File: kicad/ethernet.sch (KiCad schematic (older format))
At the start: 48 parts, among them U2 NUP4114UPXV6T1G, U3 NUP4114UPXV6T1G, X1 L829-1J1T-43

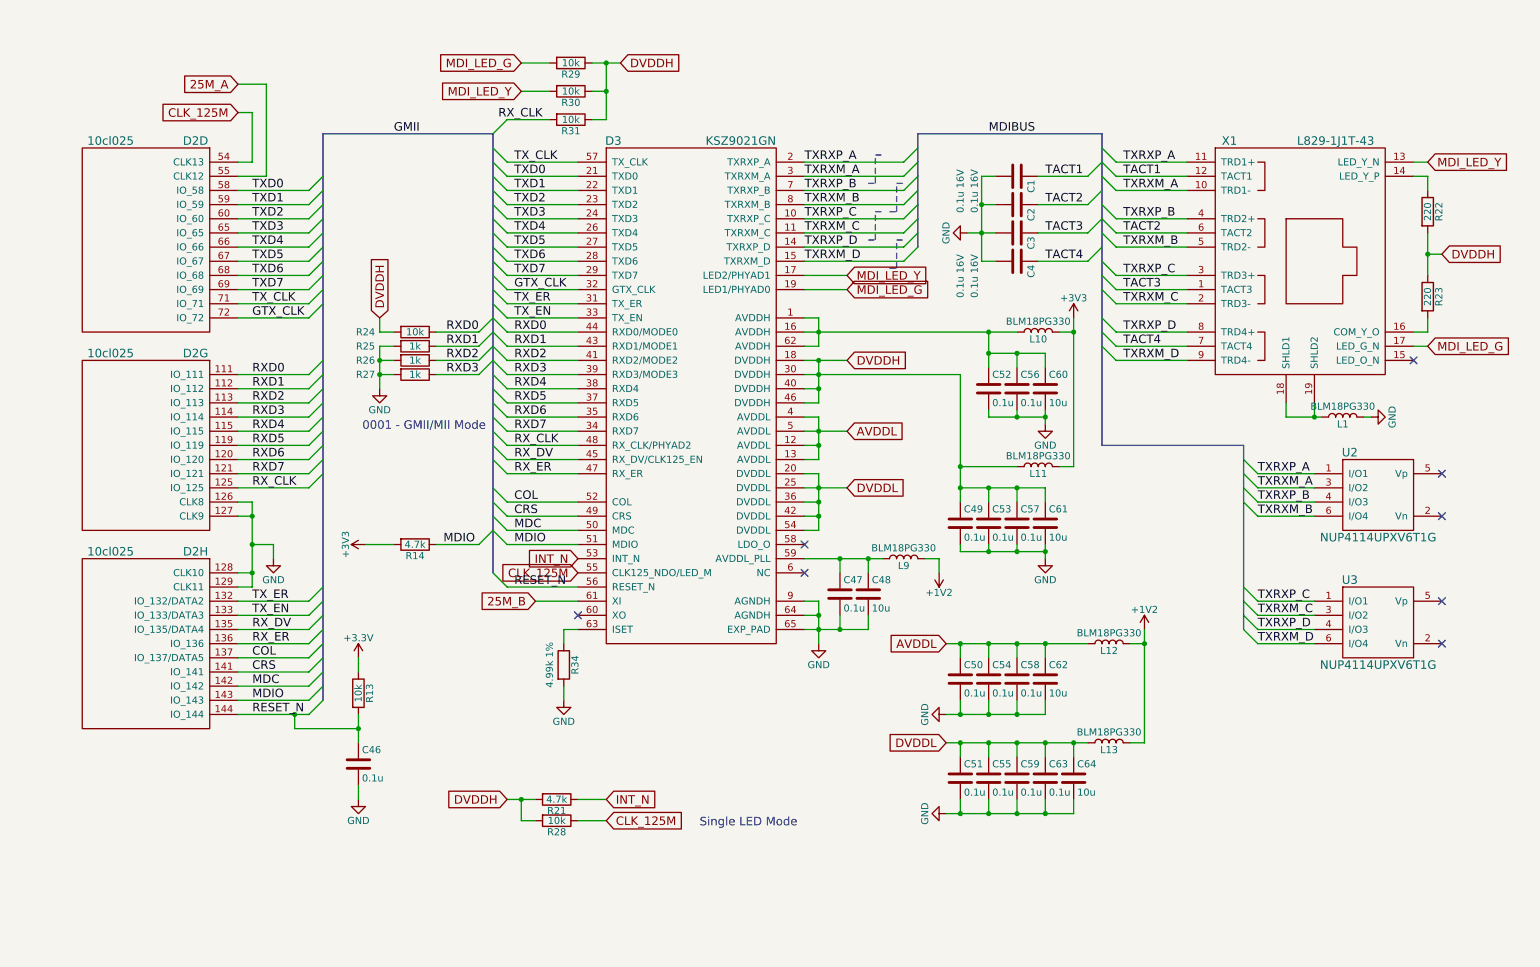
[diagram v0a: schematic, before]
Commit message: Project translated to template "Raspberry Pi HAT" Added library files from template. Renamed refdes. Changed placement for all components
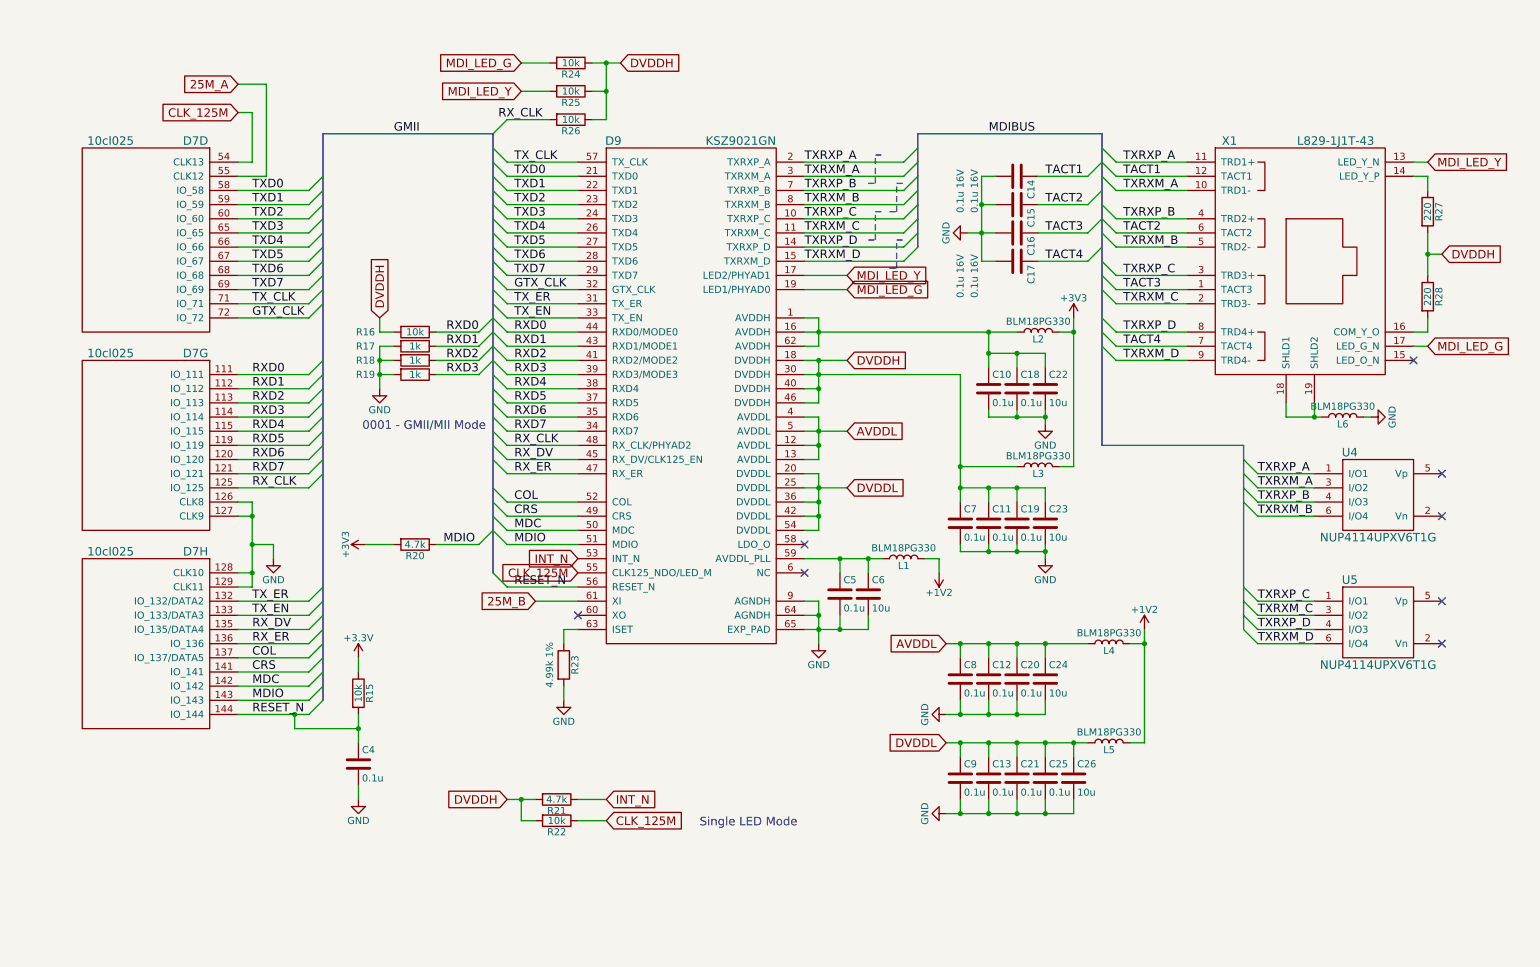
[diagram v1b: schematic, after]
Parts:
- renumbered C52 to C10, C53 to C11, C54 to C12, C55 to C13, C1 to C14, C2 to C15, C3 to C16, C4 to C17, C56 to C18, C57 to C19, C58 to C20, C59 to C21, C60 to C22, C61 to C23, C62 to C24, C63 to C25, C64 to C26, C46 to C4, C47 to C5, C48 to C6, C49 to C7, C50 to C8, C51 to C9, D2 to D7, D3 to D9, L9 to L1, L10 to L2, L11 to L3, L12 to L4, L13 to L5, L1 to L6, R13 to R15, R24 to R16, R25 to R17, R26 to R18, R27 to R19, R14 to R20, R28 to R22, R34 to R23, R29 to R24, R30 to R25, R31 to R26, R22 to R27, R23 to R28, U2 to U4, U3 to U5

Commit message: Schematics updated for correct BOM generation Corrected RefDes (not renumbered yet) PCB updated (not routed) Added 3d models for new components Added folder assy (empty) Added folder bom Added BOM file (bom/BOM_fpgagigepi.xls) Added datasheet for ocscillator 25MHz (datasheets/ASEMB.pdf)
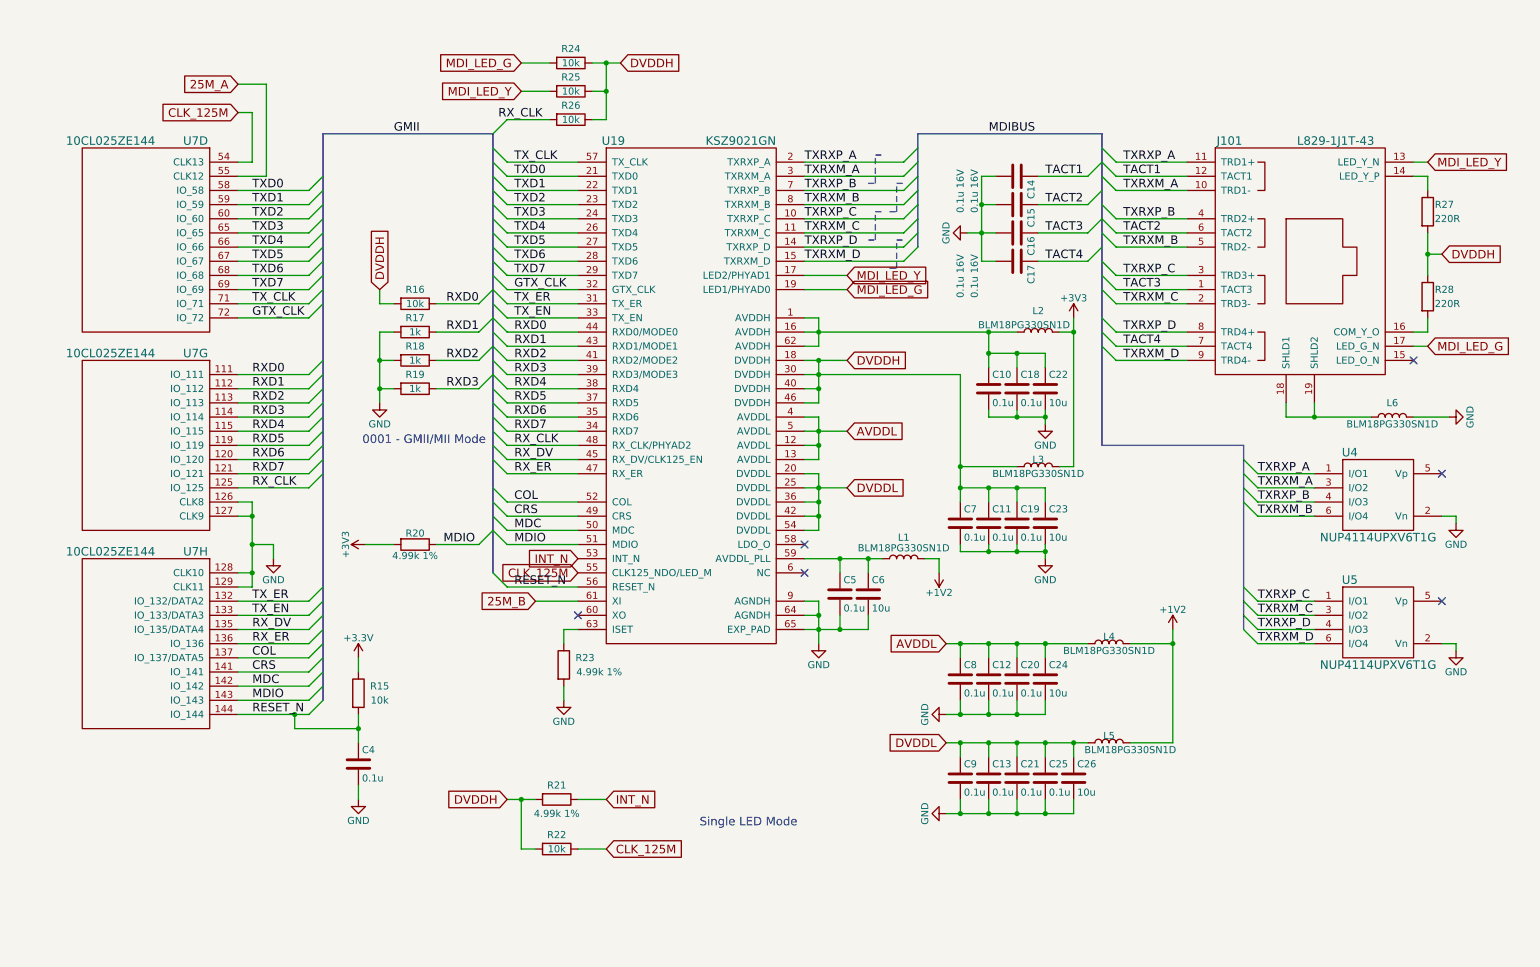
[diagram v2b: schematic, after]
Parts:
- C10, C11, C12, C13, C14, C15, C16, C17, C18, C19, C20, C21, C22, C23, C24, C25, C26, C4, C5, C6, C7, C8, C9: footprint Capacitors_SMD:C_0603_HandSoldering -> Capacitors_SMD:C_0603
- L1, L2, L3, L4, L5, L6: value BLM18PG330 -> BLM18PG330SN1D; footprint Inductors_SMD:L_0603_HandSoldering -> Inductors_SMD:L_0603
- R15, R16, R17, R18, R19, R22, R23, R24, R25, R26: footprint Resistors_SMD:R_0603_HandSoldering -> Resistors_SMD:R_0603
- R20, R21: value 4.7k -> 4.99k 1%; footprint Resistors_SMD:R_0603_HandSoldering -> Resistors_SMD:R_0603
- R27, R28: value 220 -> 220R; footprint Resistors_SMD:R_0603_HandSoldering -> Resistors_SMD:R_0603
- U7: renamed from D7; value 10cl025 -> 10CL025ZE144
- renumbered X1 to J101, D9 to U19
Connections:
- net GND: now also U4.2 (Vn), U5.2 (Vn)
- no-connect marks 8 -> 6
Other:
- moved on the sheet: L6, R16, R17, R19, R22

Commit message: Corrected path for schematics Renumbered components Remaped GMII connections to other banks PCB updated - final placement for major components and some conn routed Corrected 3d models Add text Cyclone 10LP Added 3d models for new components Added folder assy (empty) Added folder bom Added BOM file (bom/BOM_fpgagigepi.xls)
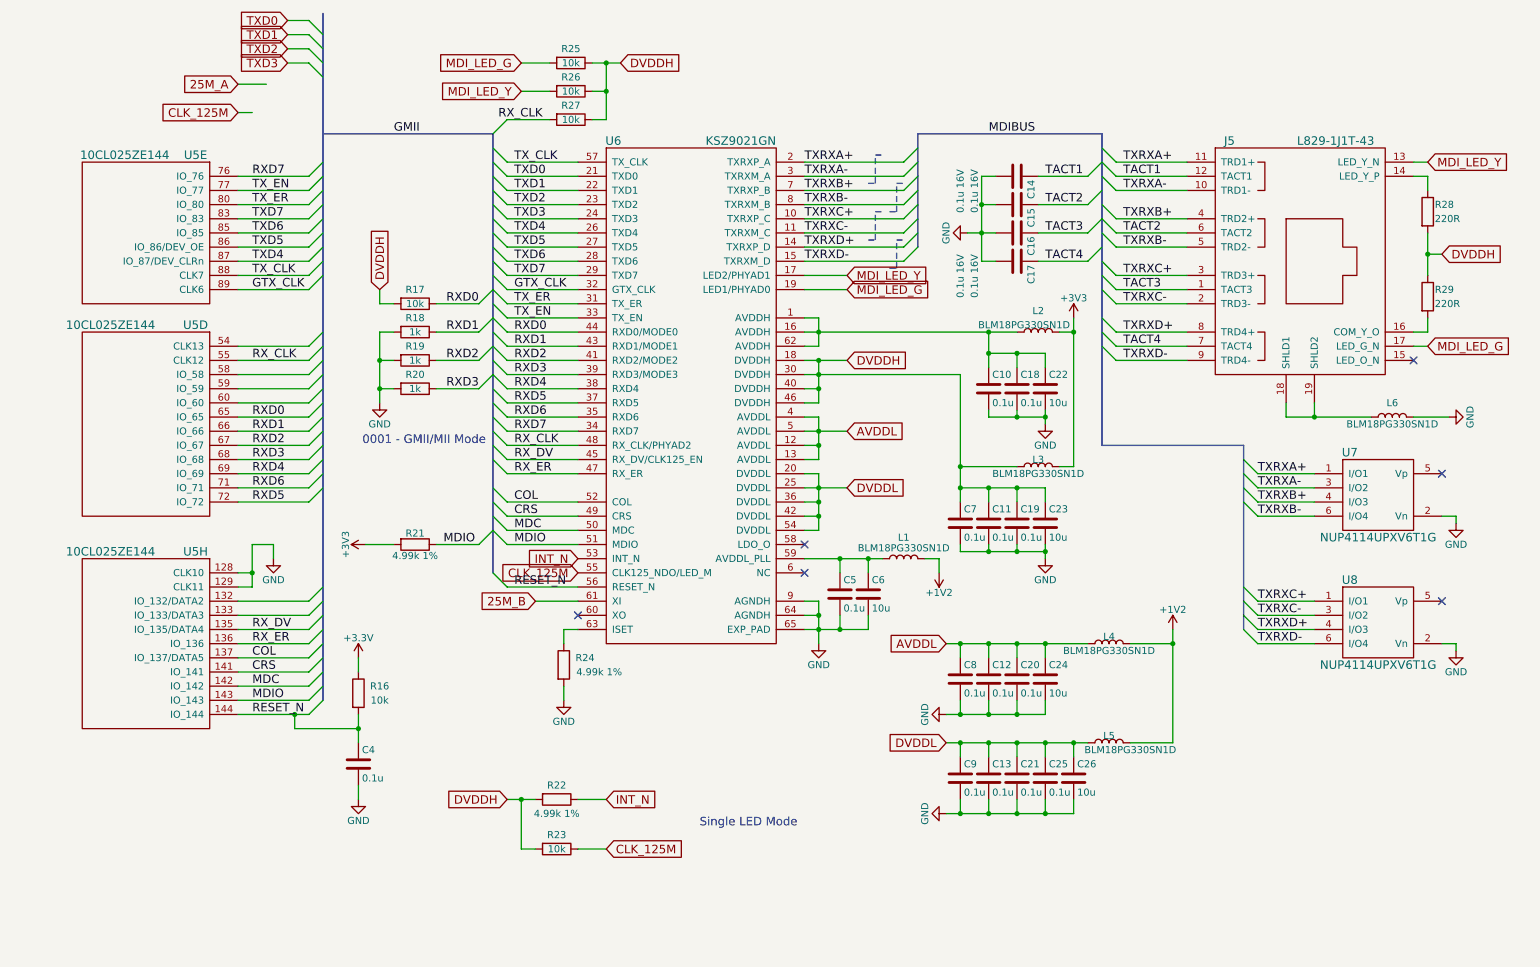
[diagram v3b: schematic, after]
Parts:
- renumbered J101 to J5, R15 to R16, R16 to R17, R17 to R18, R18 to R19, R19 to R20, R20 to R21, R21 to R22, R22 to R23, R23 to R24, R24 to R25, R25 to R26, R26 to R27, R27 to R28, R28 to R29, U7 to U5, U19 to U6, U4 to U7, U5 to U8
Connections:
- net 25M_A: no longer U5.55 (CLK12)
- net CLK_125M: no longer U5.54 (CLK13)
- net GND: no longer U5.126 (CLK8), U5.127 (CLK9)
- net GTX_CLK: now also U5.89 (CLK6); no longer U5.72 (IO_72)
- net RXD0: now also U5.65 (IO_65); no longer U5.111 (IO_111)
- net RXD1: now also U5.66 (IO_66); no longer U5.112 (IO_112)
- net RXD2: now also U5.67 (IO_67); no longer U5.113 (IO_113)
- net RXD3: now also U5.68 (IO_68); no longer U5.114 (IO_114)
- net RXD4: now also U5.69 (IO_69); no longer U5.115 (IO_115)
- net RXD5: now also U5.72 (IO_72); no longer U5.119 (IO_119)
- net RXD6: now also U5.71 (IO_71); no longer U5.120 (IO_120)
- net RXD7: now also U5.76 (IO_76); no longer U5.121 (IO_121)
- net RX_CLK: now also U5.55 (CLK12); no longer U5.125 (IO_125)
- net TXD0: no longer U5.58 (IO_58)
- net TXD1: no longer U5.59 (IO_59)
- net TXD2: no longer U5.60 (IO_60)
- net TXD3: no longer U5.65 (IO_65)
- net TXD4: now also U5.87 (IO_87/DEV_CLRn); no longer U5.66 (IO_66)
- net TXD5: now also U5.86 (IO_86/DEV_OE); no longer U5.67 (IO_67)
- net TXD6: now also U5.85 (IO_85); no longer U5.68 (IO_68)
- net TXD7: now also U5.83 (IO_83); no longer U5.69 (IO_69)
- net TX_CLK: now also U5.88 (CLK7); no longer U5.71 (IO_71)
- net TX_EN: now also U5.77 (IO_77); no longer U5.133 (IO_133/DATA3)
- net TX_ER: now also U5.80 (IO_80); no longer U5.132 (IO_132/DATA2)
- net TXRXM_A renamed TXRXA-
- net TXRXM_B renamed TXRXB-
- net TXRXM_C renamed TXRXC-
- net TXRXM_D renamed TXRXD-
- net TXRXP_A renamed TXRXA+
- net TXRXP_B renamed TXRXB+
- net TXRXP_C renamed TXRXC+
- net TXRXP_D renamed TXRXD+

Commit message: Replaced clock buffer NB3L553DR2G to cdclvc1102 Added datasheet for cdclvc1102 Added components cdclvc1102pw in library_cache Remaped cyclone-to-40-pin-header connections Updated schematics Updated PCB - all signal routed. Power connections not routed Updated BOM file (non-altium format)
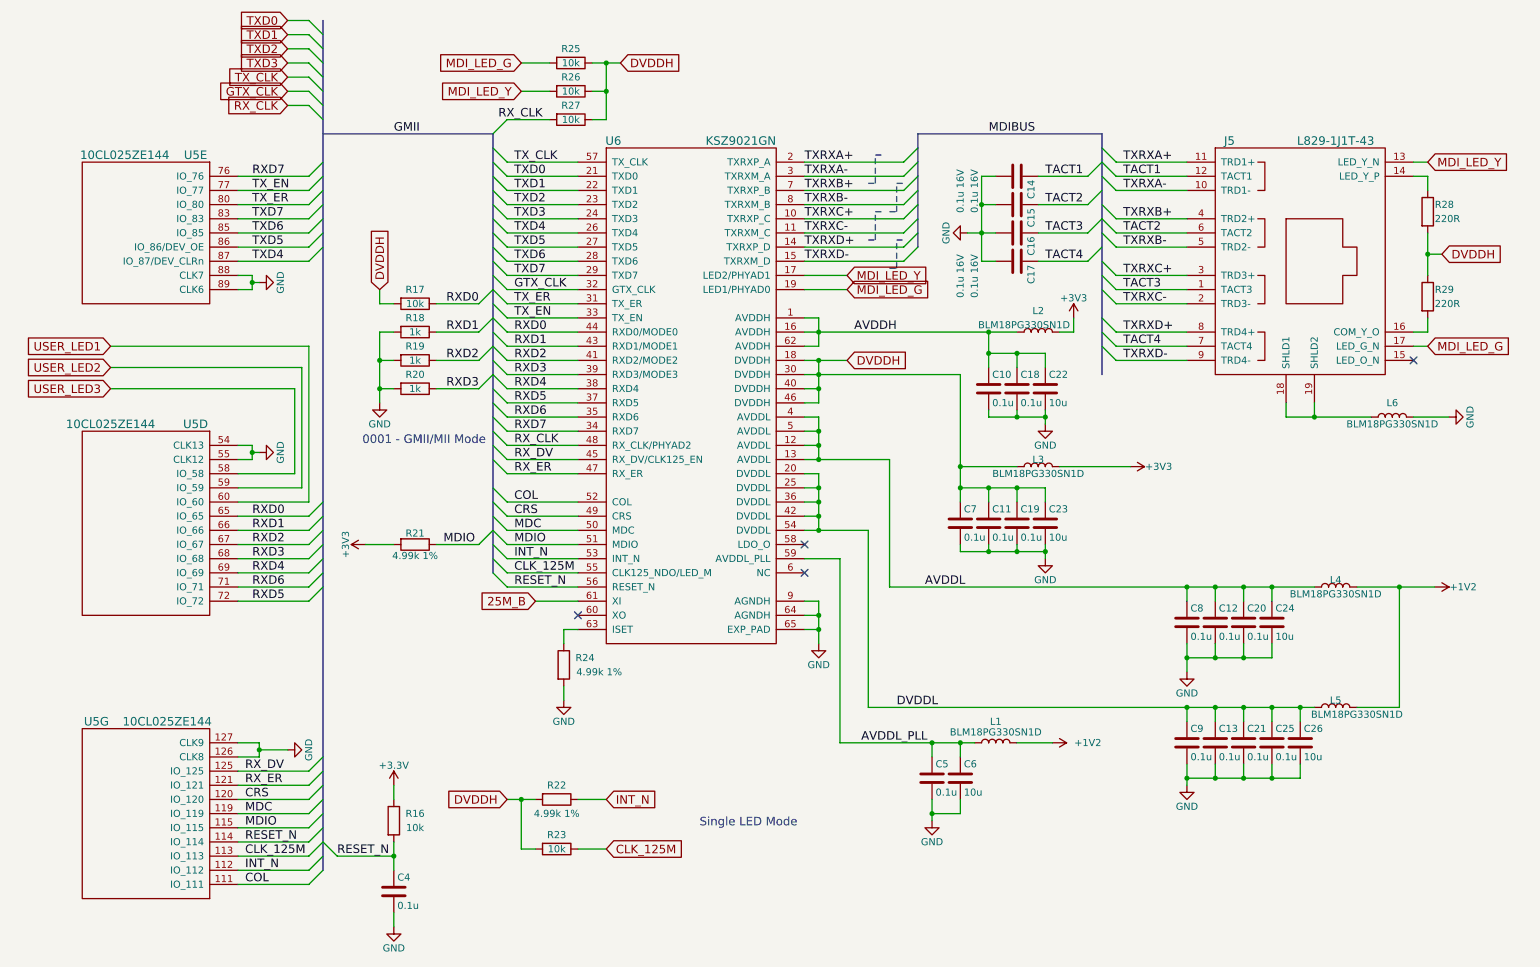
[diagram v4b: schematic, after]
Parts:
- removed U7, U8: NUP4114UPXV6T1G, library:SOT-563-6, symbol NUP4114UPXV6T1G
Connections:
- net CLK_125M: now also U5.113 (IO_113)
- net COL: now also U5.111 (IO_111); no longer U5.137 (IO_137/DATA5)
- net CRS: now also U5.120 (IO_120); no longer U5.141 (IO_141)
- net GND: now also U5.126 (CLK8), U5.127 (CLK9), U5.54 (CLK13), U5.55 (CLK12), U5.88 (CLK7), U5.89 (CLK6); no longer U5.128 (CLK10), U5.129 (CLK11)
- net GTX_CLK: no longer U5.89 (CLK6)
- net INT_N: now also U5.112 (IO_112)
- net MDC: now also U5.119 (IO_119); no longer U5.142 (IO_142)
- net MDIO: now also U5.115 (IO_115); no longer U5.143 (IO_143)
- net RESET_N: now also U5.114 (IO_114); no longer U5.144 (IO_144)
- net RX_CLK: no longer U5.55 (CLK12)
- net RX_DV: now also U5.125 (IO_125); no longer U5.135 (IO_135/DATA4)
- net RX_ER: now also U5.121 (IO_121); no longer U5.136 (IO_136)
- net TX_CLK: no longer U5.88 (CLK7)
- net AVDDH: now reaches C10.1, C18.1, C22.1, L2.1, U6.1 (AVDDH), U6.16 (AVDDH), U6.62 (AVDDH)
- net AVDDL_PLL: now reaches C5.1, C6.1, L1.1, U6.59 (AVDDL_PLL)
- net USER_LED3: now reaches U5.58 (IO_58)
- net USER_LED2: now reaches U5.59 (IO_59)
- net USER_LED1: now reaches U5.60 (IO_60)
- no-connect marks 6 -> 4
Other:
- moved on the sheet: C12, C13, C20, C21, C24, C25, C26, C4, C5, C6, C8, C9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
